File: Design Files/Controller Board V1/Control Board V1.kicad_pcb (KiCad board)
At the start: 2 copper layers, 75 x 125 mm, 35 parts, among them J1 XT30PW-M, J2 XT30PW-M, J3 XT30PW-M, J4 XT30PW-M, J5 XT30PW-M, J6 XT30PW-M, J7 XT30PW-F, J8 SM04B-GHS-TB_LF__SN_-, Q1 LMG5200, U1 LMR51420XDDCR

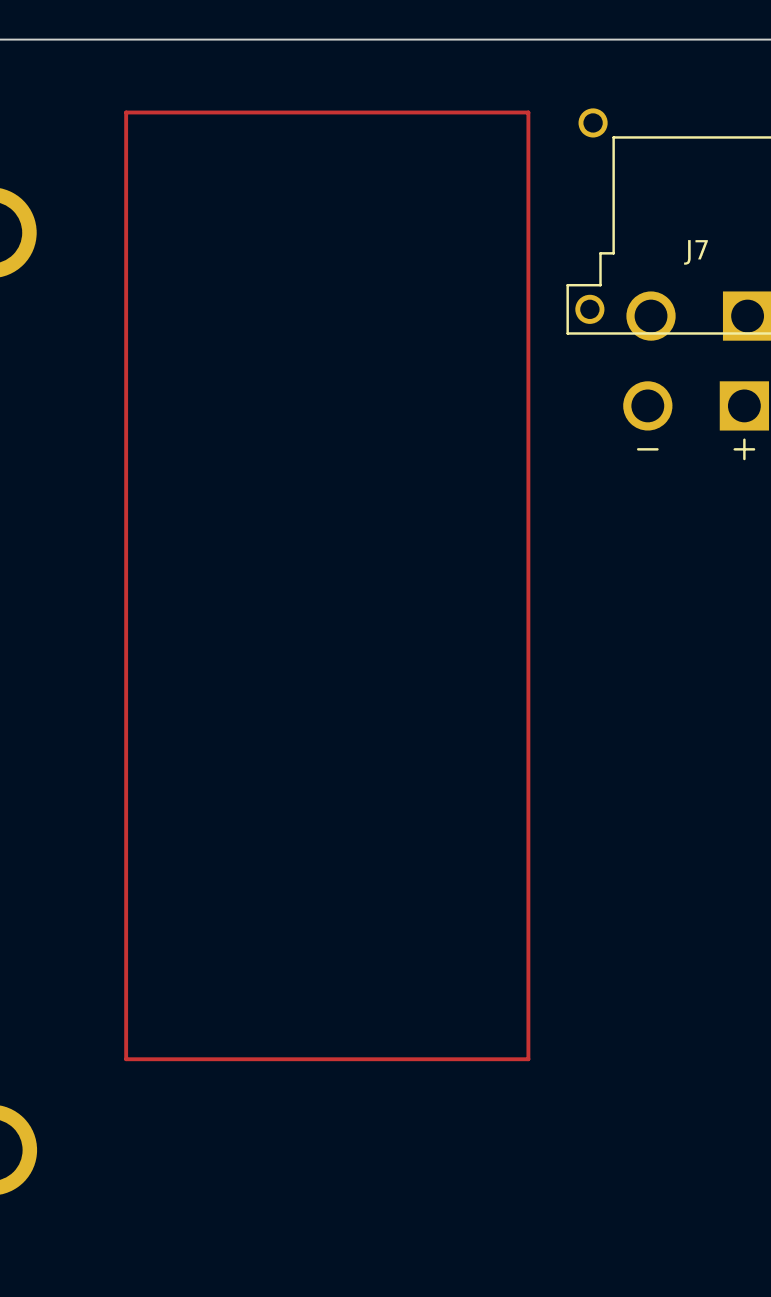
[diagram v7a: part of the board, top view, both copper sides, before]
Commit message: Pico Schematic Started
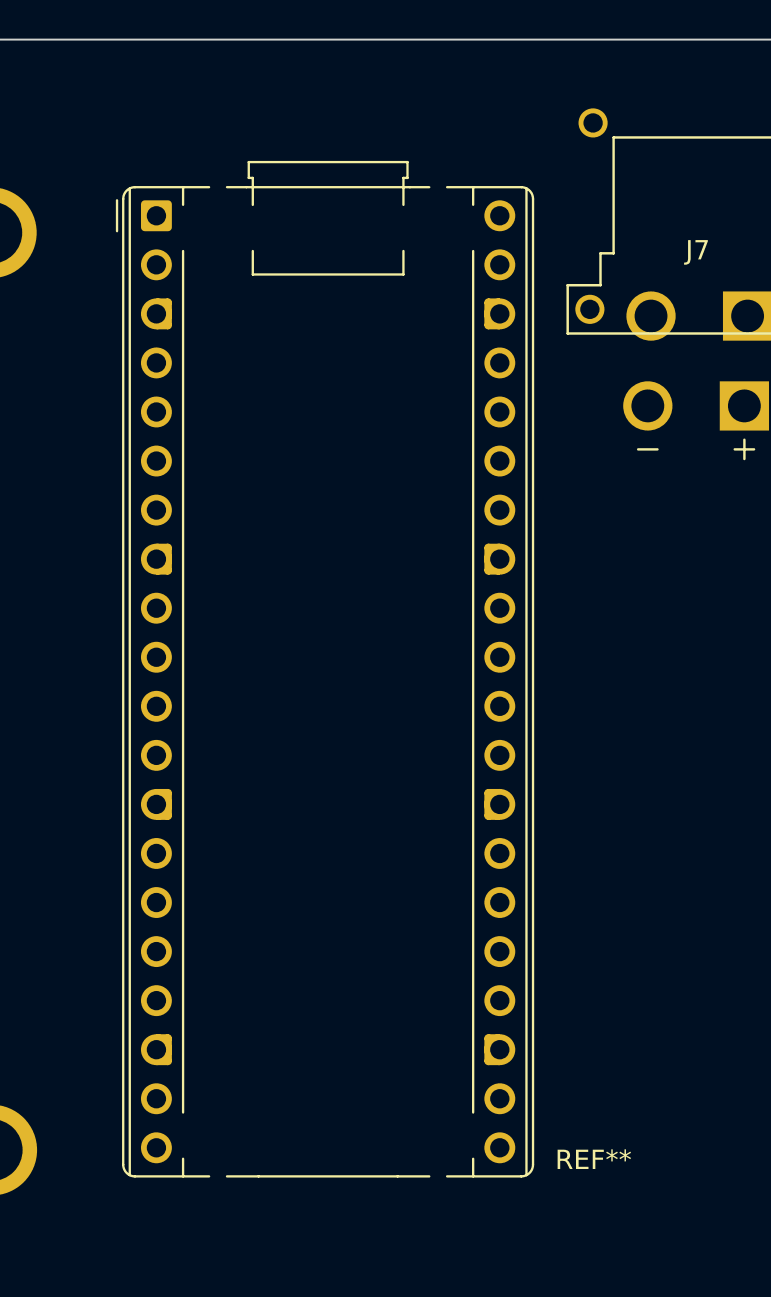
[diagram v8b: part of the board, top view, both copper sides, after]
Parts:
- added REF**: RaspberryPi_Pico_Common_THT, Module:RaspberryPi_Pico_Common_THT, F.Cu at (81.1, 46.6)
